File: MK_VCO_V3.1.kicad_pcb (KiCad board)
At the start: 2 copper layers, 212.9 x 110 mm, 92 parts, among them J1 CV, J10 InJackP, J11 PWMPotB, J12 PWMPotP, J13 PWMJackB, J14 PWMJackP, J15 OutJackB, J16 OutJackP, J2 FM, J3 SAW, J4 PWM, J5 PUL, J6 TRI, J7 InPotB, J8 InPotP, J85 Eurorack Conn., J9 InJackB, Q1 BC558, Q2 BC548, U1 40106, U2 TL074, U3 TL072

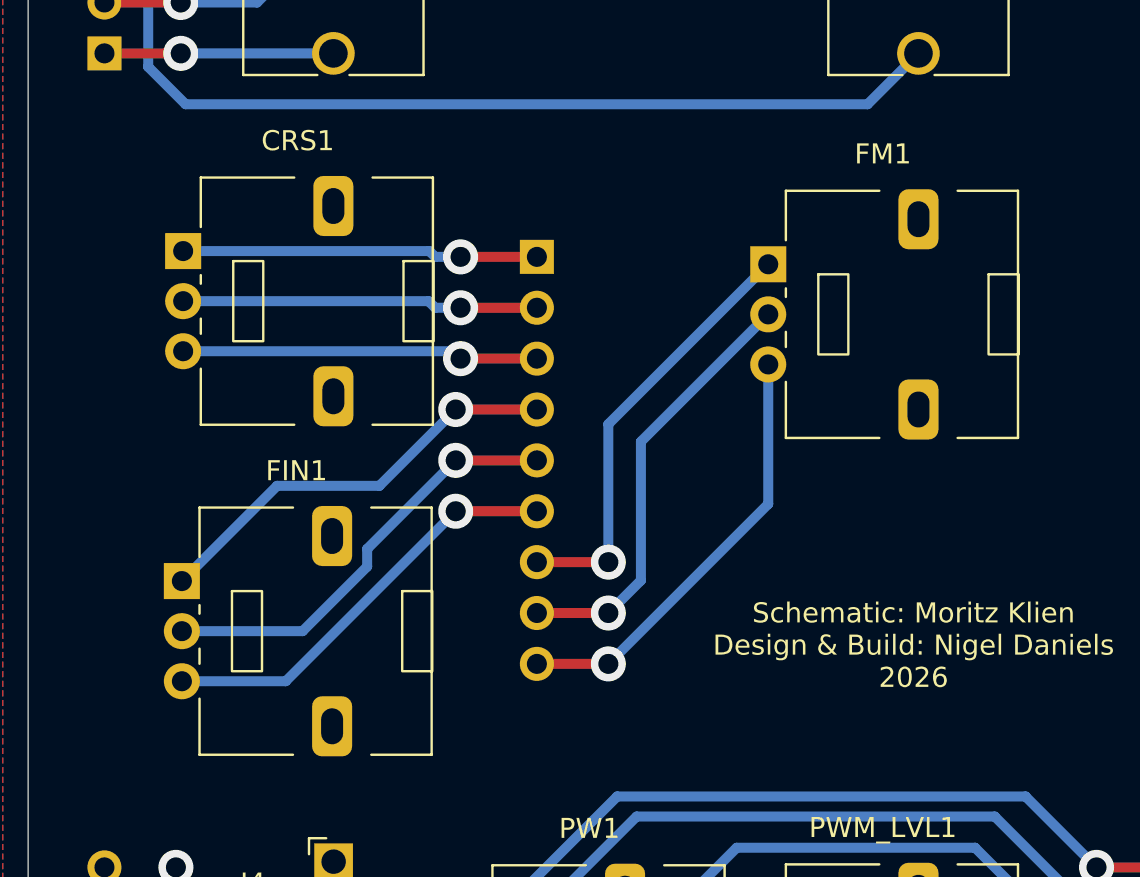
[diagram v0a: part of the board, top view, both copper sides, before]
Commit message: Fixed inverted pots
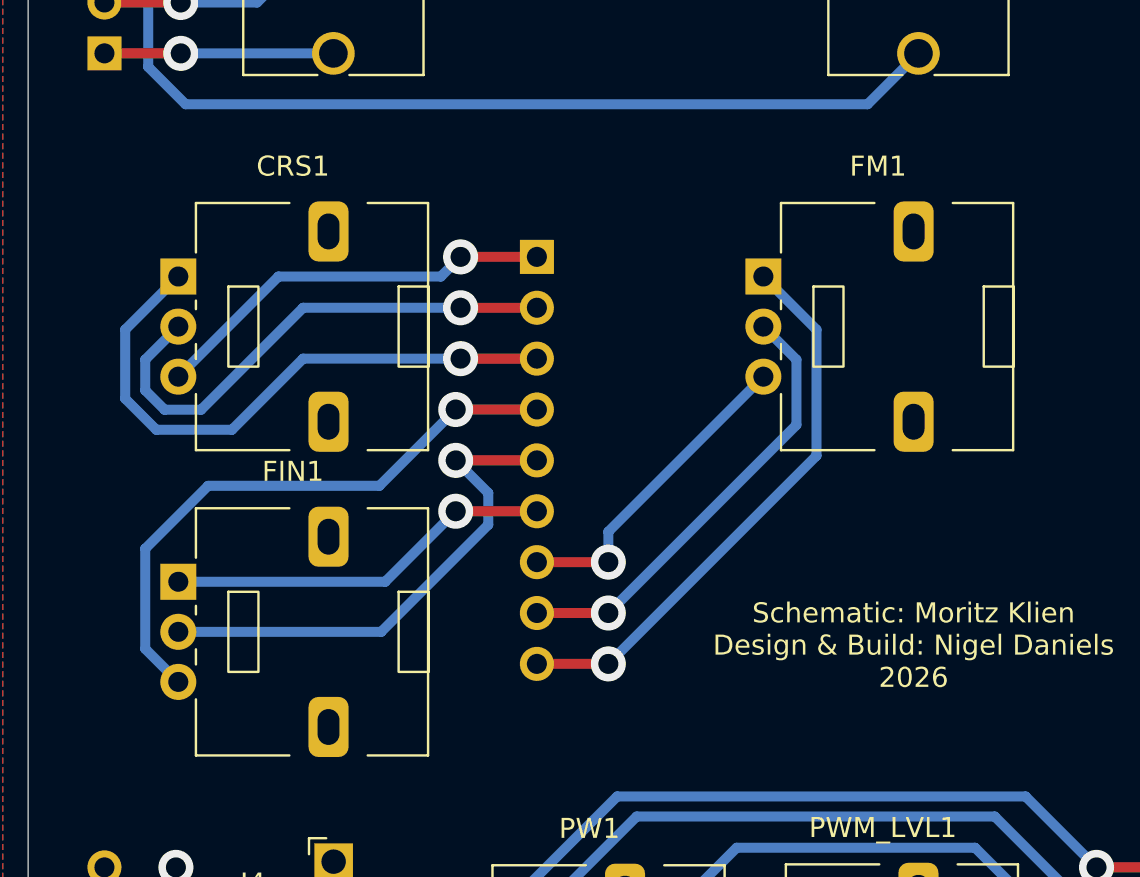
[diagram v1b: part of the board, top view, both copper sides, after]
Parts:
- D1, D2, D3: value D -> 1N4148
- J10: value InJackP -> 1x4 m
- J11: value PWMPotB -> 1x6 f
- J12: value PWMPotP -> 1x6 m
- J13: value PWMJackB -> 1x2 f
- J14: value PWMJackP -> 1x2 m
- J15: value OutJackB -> 1x6 f
- J16: value OutJackP -> 1x6 m
- J7: value InPotB -> 1x9 f
- J8: value InPotP -> 1x9 m
- J9: value InJackB -> 1x4 f
- moved CRS1 1.29 mm to (124.6, 61.9)
- moved FM1 0.66 mm to (153.8, 61.9)
- moved FIN1 0.18 mm to (124.6, 77.2)
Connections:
- CRS1 pad 1: Net-(J8-Pin_1) -> Net-(J8-Pin_3)
- CRS1 pad 3: Net-(J8-Pin_3) -> Net-(J8-Pin_1)
- FIN1 pad 1: Net-(J8-Pin_4) -> Net-(J8-Pin_6)
- FIN1 pad 3: Net-(J8-Pin_6) -> Net-(J8-Pin_4)
- FM1 pad 1: Net-(J8-Pin_7) -> Net-(J8-Pin_9)
- FM1 pad 3: Net-(J8-Pin_9) -> Net-(J8-Pin_7)
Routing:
- net Net-(J8-Pin_3): track 17.8 -> 29.9 mm
- net Net-(J8-Pin_4): track 21.3 -> 29.8 mm
- net Net-(J8-Pin_2): track 17.8 -> 25.9 mm
- net Net-(J8-Pin_9): track 21.8 -> 28.3 mm
- net Net-(J8-Pin_7): track 21.7 -> 16.0 mm
- net Net-(J8-Pin_5): track 21.8 -> 25.6 mm
- net Net-(J8-Pin_1): track 17.8 -> 20.4 mm
- net Net-(J8-Pin_6): track 21.2 -> 19.4 mm
- net Net-(J8-Pin_8): track 21.8 -> 22.4 mm
